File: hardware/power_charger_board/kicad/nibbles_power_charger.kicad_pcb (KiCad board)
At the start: 4 copper layers, 30 x 100 mm, 125 parts, among them J10 JST-GH 8 vertical (cable to t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, J11 JST-GH 6 vertical (I2C port 2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, J2 XT30PW-M (dock power, from th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, J3 XT30 (pack, from 4S BMS), J4 NTC 103AT on the cells (JST-G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, J5 XT30 (to the 5 V lighting con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, J6 To the 3.49 (stacked headers), J7 BM02B-GHS-TBT (dock data + de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, J8 BM02B-GHS-TBT (dock LED, pane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, J9 JST-GH 6 vertical (keypad por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, Q5 30V N-FET >= 15 A, Q6 30V N-FET >= 15 A, Q7 2N7002, Q8 2N7002, Q9 30V N-FET >= 15 A, U2 BQ25798RQMR, U3 LM74700-Q1 (dock), U4 LM74700-Q1 (pack), U5 TPS259827ONRGET, U6 INA226AIDGSR, U7 TPS62933DRLR, U8 TCA9534PWR, U9 LM74700-Q1 (LEMO)

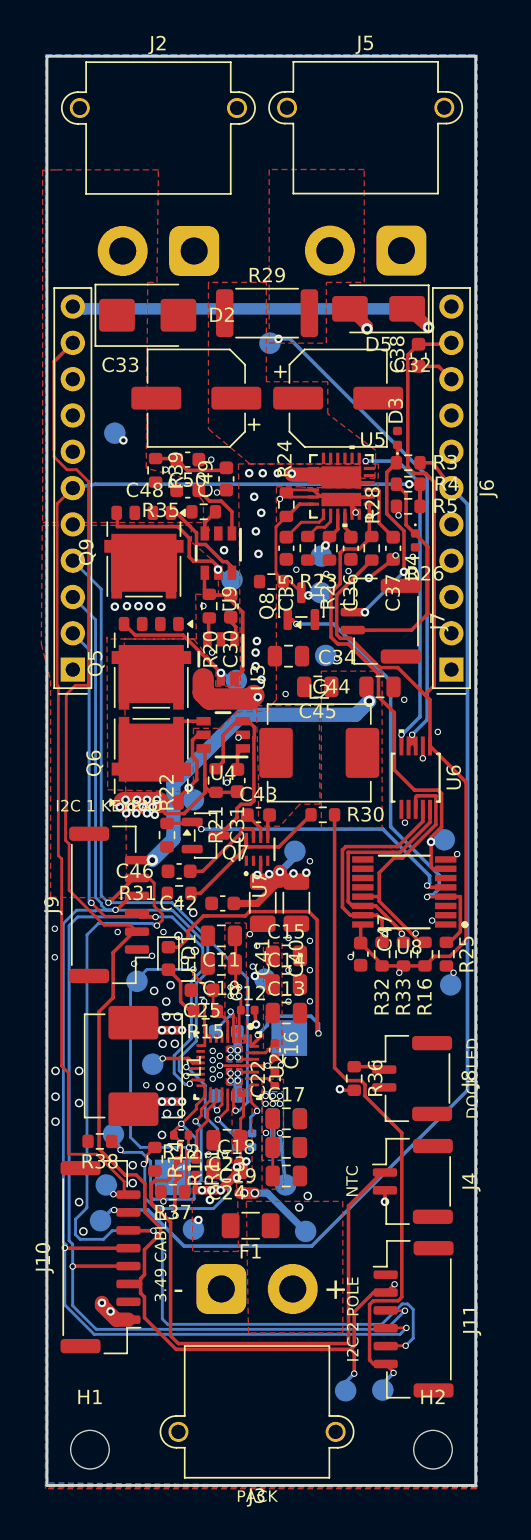
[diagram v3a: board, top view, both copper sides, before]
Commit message: Power + charger board: silkscreen laid out, shark LED outline logo
- Silkscreen: every reference beside its own part (1.0 mm, 0.8 mm where
  tight), clear of pads, other silk, the edge and part bodies; XT30
  references and job labels on the bottom by their pins; the 31 dense
  0402/0603 parts that have no room keep their references on Fab only
- Logo: the shark's blue LED tube traced from a side render of the totem
  model, with the eye; nibbles:Nibbles_Shark_Logo_12mm/15mm/20mm
  footprints (filled F.Silkscreen polygons, board-only) and SVG/PNG in
  logo/; the 12 mm one placed on the board

Co-Authored-By: Claude Opus 5.5 <noreply@anthropic.com>
Claude-Session: https://claude.ai/code/session_01UUhpevE9ZSCJvyu3edQmf9
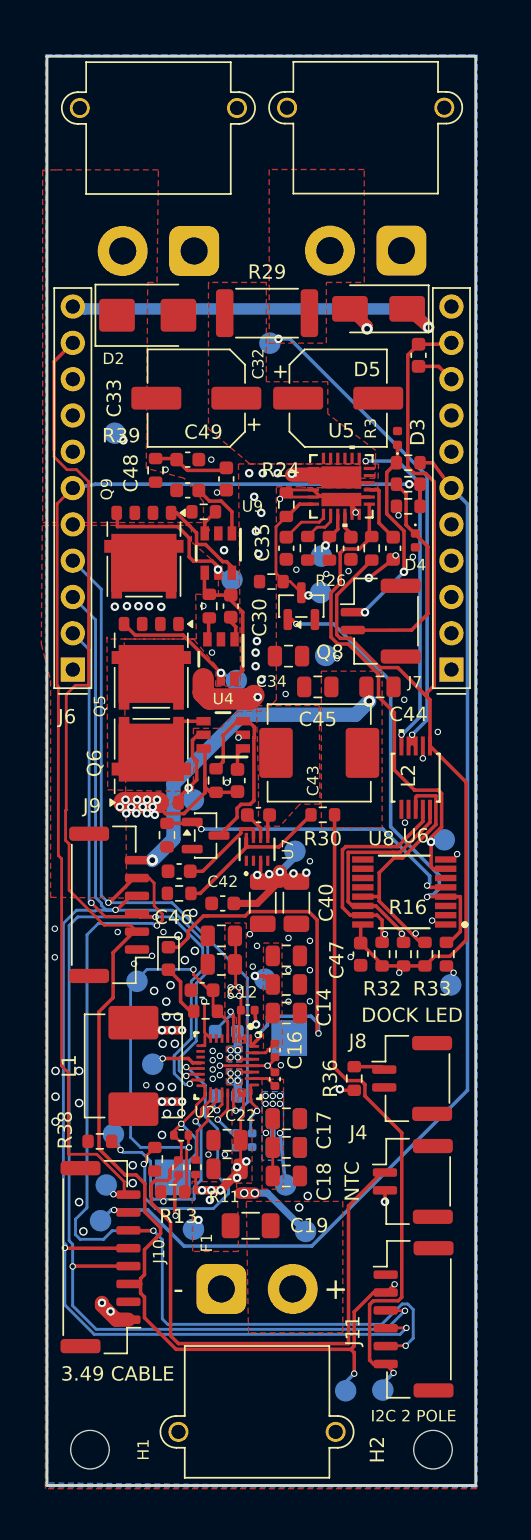
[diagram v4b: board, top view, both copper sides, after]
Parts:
- added LOGO: Nibbles_Shark_Logo_12mm, nibbles:Nibbles_Shark_Logo_12mm, B.Cu at (52.7, 67.1)
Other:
- board text added: "NIBBLES Base Controller v1.0"
- board text removed: "NIBBLES POWER + CHARGER rev A 2026-10"

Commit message: Power + charger board: 20 mm shark logo on the bottom, current eye
Co-Authored-By: Claude Opus 5.5 <noreply@anthropic.com>
Claude-Session: https://claude.ai/code/session_01UUhpevE9ZSCJvyu3edQmf9
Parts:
- removed the LOGO at (52.7, 67.1)
- added LOGO: Nibbles_Shark_Logo_20mm, nibbles:Nibbles_Shark_Logo_20mm, B.Cu at (47.6, 91.2)
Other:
- board text added: "Nibbles Base Controller v1.0 Dreamstate 2026"
- board text removed: "NIBBLES Base Controller v1.0"

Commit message: Power + charger board: JLCPCB fab files, LCSC and DigiKey orders
- fab/export.sh: gerbers, drills, JLCPCB BOM/CPL after ERC, DRC and parity
  checks, plus LCSC and DigiKey order lists (DigiKey parts from
  digikey_map.csv; what DigiKey can't supply goes to an LCSC gaps list)
- LCSC fields on every part, picked to be in stock at LCSC for a hand build
- eFuse timing caps set: C35 ITIMER 22n, C36 RETRY_DLY 22n, C37 dVdt 47n;
  R27 IMON 1k

Co-Authored-By: Claude Opus 5.5 <noreply@anthropic.com>
Claude-Session: https://claude.ai/code/session_01UUhpevE9ZSCJvyu3edQmf9
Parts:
- C35: value 10nF (TBD) -> 22nF
- C36: value 100nF (TBD) -> 22nF
- C37: value 22nF (TBD) -> 47nF
- R27: value TBD (IMON) -> 1k
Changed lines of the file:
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@@
 			)
 		)
-		(property "Value" "10nF (TBD)"
+		(property "Value" "22nF"
 			(at 0 1.43 90)
 			(layer "F.Fab")
@@
 			)
 		)
-		(property "Value" "22nF (TBD)"
+		(property "Value" "47nF"
 			(at 0 1.43 90)
 			(layer "F.Fab")
@@
 			)
 		)
-		(property "Value" "TBD (IMON)"
+		(property "Value" "1k"
 			(at 0 1.43 90)
 			(layer "F.Fab")
@@
 			)
 		)
-		(property "Value" "100nF (TBD)"
+		(property "Value" "22nF"
 			(at 0 1.43 90)
 			(layer "F.Fab")
